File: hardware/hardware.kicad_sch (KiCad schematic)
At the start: 39 parts, among them J1 USB_C_Receptacle_USB2.0, J2 Conn_01x12_Pin, J4 Conn_01x12_Pin, SW1 RST, SW2 BOOT, U1 ESP32-C3-MINI-1, U2 CH217K, U3 AMS1117-3.3, U4 DHT11, U5 BMP280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

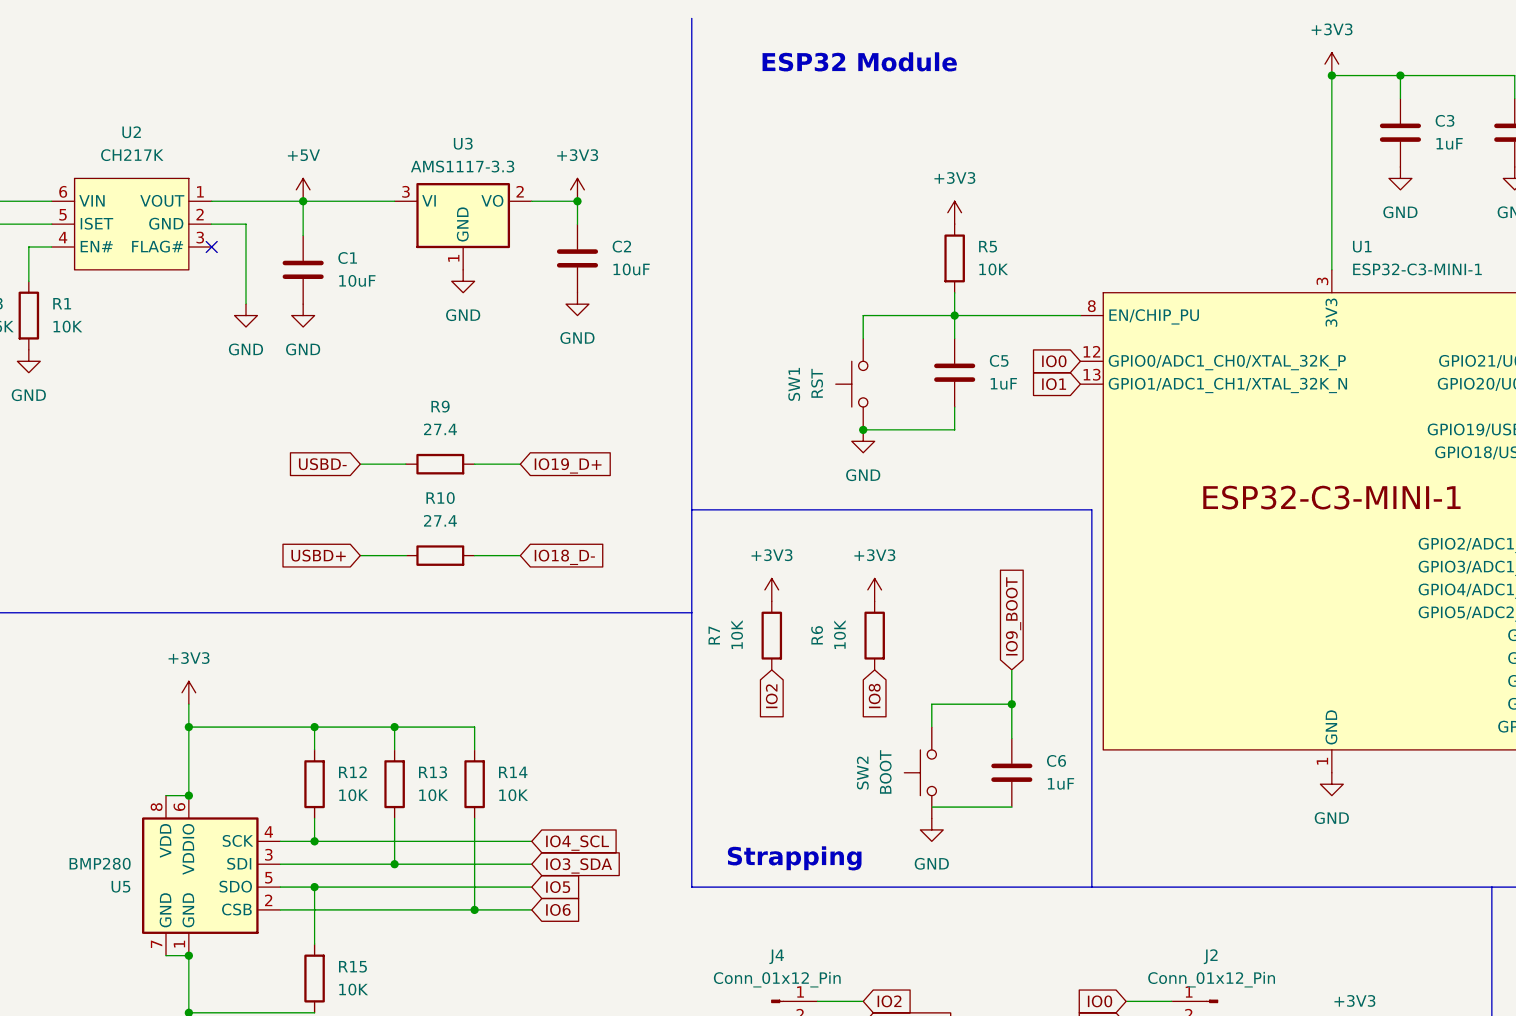
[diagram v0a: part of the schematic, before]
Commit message: Auto routing for PCB by free-routing.
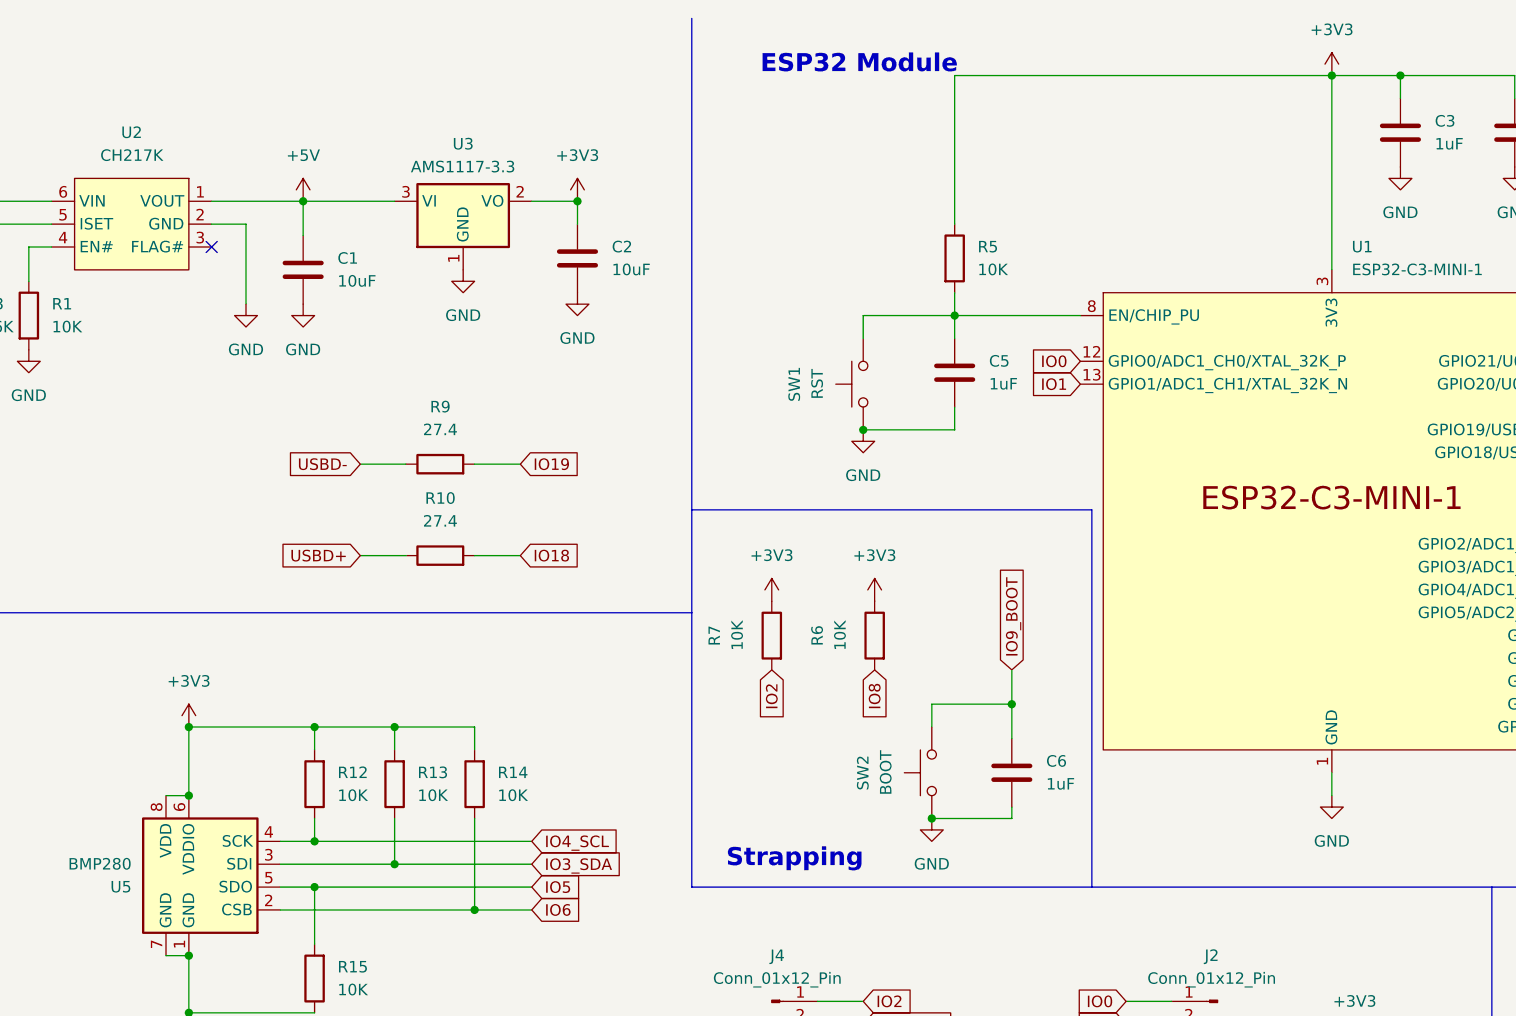
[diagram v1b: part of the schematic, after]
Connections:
- net IO18_D- is gone; now on net IO18: R10.2
- net IO19_D+ is gone; now on net IO19: R9.2
- net GND: now also C6.2

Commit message: Draft version to enable stepper.
And have some changes on KiCad data, may have something wrong. Let's just keep them now.
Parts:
- removed R1: 10K, Resistor_SMD:R_0402_1005Metric, symbol Device:R
- removed R3: 56K, Resistor_SMD:R_0402_1005Metric, symbol Device:R
- removed U2: CH217K, Package_TO_SOT_SMD:SOT-23-6, symbol wch_mcu_peripheral:CH217K
- C1, C2: footprint Capacitor_SMD:C_0402_1005Metric -> Capacitor_SMD:C_0805_2012Metric
- C7: value 0.1uF -> 100nF
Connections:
- net +5V: now also J1.A4 (VBUS), J1.A9 (VBUS), J1.B4 (VBUS), J1.B9 (VBUS)
- no-connect marks 6 -> 5
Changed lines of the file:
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@@
   (no_connect (at 41.91 59.69))
   (no_connect (at 271.78 123.19))
-  (no_connect (at 93.98 36.83))
   (wire (pts (xy 26.67 158.75) (xy 21.59 158.75))
     (stroke (width 0) (type default))
@@
     (stroke (width 0) (type default))
   )
-  (wire (pts (xy 66.04 34.29) (xy 66.04 40.64))
-    (stroke (width 0) (type default))
-  )
   (wire (pts (xy 104.14 31.75) (xy 104.14 35.56))
     (stroke (width 0) (type default))
@@
     (stroke (width 0) (type default))
   )
-  (wire (pts (xy 97.79 34.29) (xy 97.79 43.18))
-    (stroke (width 0) (type default))
-  )
   (wire (pts (xy 226.06 17.78) (xy 238.76 17.78))
     (stroke (width 0) (type default))
@@
     (stroke (width 0) (type default))
   )
-  (wire (pts (xy 93.98 34.29) (xy 97.79 34.29))
-    (stroke (width 0) (type default))
-  )
   (wire (pts (xy 246.38 59.69) (xy 248.92 59.69))
     (stroke (width 0) (type default))
@@
     (stroke (width 0) (type default))
   )
-  (wire (pts (xy 73.66 36.83) (xy 73.66 40.64))
-    (stroke (width 0) (type default))
-  )
   (wire (pts (xy 101.6 110.49) (xy 123.19 110.49))
     (stroke (width 0) (type default))
@@
     (stroke (width 0) (type default))
   )
-  (wire (pts (xy 76.2 36.83) (xy 73.66 36.83))
-    (stroke (width 0) (type default))
-  )
   (wire (pts (xy 49.53 153.67) (xy 49.53 152.4))
     (stroke (width 0) (type default))
@@
     (stroke (width 0) (type default))
   )
-  (wire (pts (xy 41.91 31.75) (xy 76.2 31.75))
+  (wire (pts (xy 41.91 31.75) (xy 104.14 31.75))
     (stroke (width 0) (type default))
   )
@@
     (stroke (width 0) (type default))
   )
-  (wire (pts (xy 76.2 34.29) (xy 66.04 34.29))
-    (stroke (width 0) (type default))
-  )
   (wire (pts (xy 161.29 125.73) (xy 166.37 125.73))
     (stroke (width 0) (type default))
@@
   )
   (wire (pts (xy 105.41 92.71) (xy 105.41 90.17))
-    (stroke (width 0) (type default))
-  )
-  (wire (pts (xy 93.98 31.75) (xy 104.14 31.75))
     (stroke (width 0) (type default))
   )
@@
       (effects (font (size 1.27 1.27)) (justify left))
     )
-    (property "Footprint" "Capacitor_SMD:C_0402_1005Metric" (at 105.1052 43.18 0)
+    (property "Footprint" "Capacitor_SMD:C_0805_2012Metric" (at 105.1052 43.18 0)
       (effects (font (size 1.27 1.27)) hide)
     )
@@
     )
   )
-  (symbol (lib_id "Device:R") (at 73.66 44.45 0) (unit 1)
-    (in_bom yes) (on_board yes) (dnp no) (fields_autoplaced)
-    (property "Reference" "R1" (at 76.2 43.18 0)
-      (effects (font (size 1.27 1.27)) (justify left))
-    )
-    (property "Value" "10K" (at 76.2 45.72 0)
-      (effects (font (size 1.27 1.27)) (justify left))
-    )
-    (property "Footprint" "Resistor_SMD:R_0402_1005Metric" (at 71.882 44.45 90)
-      (effects (font (size 1.27 1.27)) hide)
-    )
-    (property "Datasheet" "~" (at 73.66 44.45 0)
-      (effects (font (size 1.27 1.27)) hide)
-    )
-    (pin "1")
-    (pin "2")
-    (instances
-      (project "hardware"
-        (path "/d72f8024-ddb5-42d1-8bba-6f155975e95c"
-          (reference "R1") (unit 1)
-        )
-      )
-    )
-  )
   (symbol (lib_id "Device:R") (at 58.42 63.5 0) (unit 1)
     (in_bom yes) (on_board yes) (dnp no) (fields_autoplaced)
@@
     )
   )
-  (symbol (lib_id "power:GND") (at 66.04 48.26 0) (unit 1)
-    (in_bom yes) (on_board yes) (dnp no) (fields_autoplaced)
-    (property "Reference" "#PWR01" (at 66.04 54.61 0)
-      (effects (font (size 1.27 1.27)) hide)
-    )
-    (property "Value" "GND" (at 66.04 53.34 0)
-      (effects (font (size 1.27 1.27)))
-    )
-    (property "Footprint" "" (at 66.04 48.26 0)
-      (effects (font (size 1.27 1.27)) hide)
-    )
-    (property "Datasheet" "" (at 66.04 48.26 0)
-      (effects (font (size 1.27 1.27)) hide)
-    )
-    (pin "1")
-    (instances
-      (project "hardware"
-        (path "/d72f8024-ddb5-42d1-8bba-6f155975e95c"
-          (reference "#PWR01") (unit 1)
-        )
-      )
-    )
-  )
   (symbol (lib_id "Device:R") (at 119.38 60.96 90) (unit 1)
     (in_bom yes) (on_board yes) (dnp no) (fields_autoplaced)
@@
       (effects (font (size 1.27 1.27)) (justify left))
     )
-    (property "Footprint" "Capacitor_SMD:C_0402_1005Metric" (at 135.5852 41.91 0)
+    (property "Footprint" "Capacitor_SMD:C_0805_2012Metric" (at 135.5852 41.91 0)
       (effects (font (size 1.27 1.27)) hide)
     )
@@
         (path "/d72f8024-ddb5-42d1-8bba-6f155975e95c"
           (reference "C6") (unit 1)
-        )
-      )
-    )
-  )
-  (symbol (lib_id "power:GND") (at 73.66 48.26 0) (unit 1)
-    (in_bom yes) (on_board yes) (dnp no) (fields_autoplaced)
-    (property "Reference" "#PWR03" (at 73.66 54.61 0)
-      (effects (font (size 1.27 1.27)) hide)
-    )
-    (property "Value" "GND" (at 73.66 53.34 0)
-      (effects (font (size 1.27 1.27)))
-    )
-    (property "Footprint" "" (at 73.66 48.26 0)
-      (effects (font (size 1.27 1.27)) hide)
-    )
-    (property "Datasheet" "" (at 73.66 48.26 0)
-      (effects (font (size 1.27 1.27)) hide)
-    )
-    (pin "1")
-    (instances
-      (project "hardware"
-        (path "/d72f8024-ddb5-42d1-8bba-6f155975e95c"
-          (reference "#PWR03") (unit 1)
         )
       )
@@
       (effects (font (size 1.27 1.27)) (justify left))
     )
-    (property "Value" "0.1uF" (at 62.23 166.37 0)
+    (property "Value" "100nF" (at 62.23 166.37 0)
       (effects (font (size 1.27 1.27)) (justify left))
     )
@@
     )
   )
-  (symbol (lib_id "power:GND") (at 97.79 43.18 0) (unit 1)
-    (in_bom yes) (on_board yes) (dnp no) (fields_autoplaced)
-    (property "Reference" "#PWR05" (at 97.79 49.53 0)
-      (effects (font (size 1.27 1.27)) hide)
-    )
-    (property "Value" "GND" (at 97.79 48.26 0)
-      (effects (font (size 1.27 1.27)))
-    )
-    (property "Footprint" "" (at 97.79 43.18 0)
-      (effects (font (size 1.27 1.27)) hide)
-    )
-    (property "Datasheet" "" (at 97.79 43.18 0)
-      (effects (font (size 1.27 1.27)) hide)
-    )
-    (pin "1")
-    (instances
-      (project "hardware"
-        (path "/d72f8024-ddb5-42d1-8bba-6f155975e95c"
-          (reference "#PWR05") (unit 1)
-        )
-      )
-    )
-  )
   (symbol (lib_id "power:+3V3") (at 264.16 115.57 0) (unit 1)
     (in_bom yes) (on_board yes) (dnp no) (fields_autoplaced)
@@
     )
   )
-  (symbol (lib_id "wch_mcu_peripheral:CH217K") (at 85.09 34.29 0) (mirror y) (unit 1)
-    (in_bom yes) (on_board yes) (dnp no)
-    (property "Reference" "U2" (at 85.09 24.13 0)
-      (effects (font (size 1.27 1.27)))
-    )
-    (property "Value" "CH217K" (at 85.09 26.67 0)
-      (effects (font (size 1.27 1.27)))
-    )
-    (property "Footprint" "Package_TO_SOT_SMD:SOT-23-6" (at 87.63 44.45 0)
-      (effects (font (size 1.27 1.27)) hide)
-    )
-    (property "Datasheet" "" (at 91.44 39.37 0)
-      (effects (font (size 1.27 1.27)) hide)
-    )
-    (pin "3")
-    (pin "1")
-    (pin "5")
-    (pin "6")
-    (pin "4")
-    (pin "2")
-    (instances
-      (project "hardware"
-        (path "/d72f8024-ddb5-42d1-8bba-6f155975e95c"
-          (reference "U2") (unit 1)
-        )
-      )
-    )
-  )
   (symbol (lib_id "Sensor:DHT11") (at 30.48 102.87 0) (unit 1)
     (in_bom yes) (on_board yes) (dnp no) (fields_autoplaced)
@@
         )
       )
-    )
-  )
-  (symbol (lib_id "Device:R") (at 66.04 44.45 0) (unit 1)
-    (in_bom yes) (on_board yes) (dnp no) (fields_autoplaced)
-    (property "Reference" "R3" (at 68.58 43.18 0)
-      (effects (font (size 1.27 1.27)) (justify left))
-    )
-    (property "Value" "56K" (at 68.58 45.72 0)
-      (effects (font (size 1.27 1.27)) (justify left))
-    )
-    (property "Footprint" "Resistor_SMD:R_0402_1005Metric" (at 64.262 44.45 90)
-      (effects (font (size 1.27 1.27)) hide)
-    )
-    (property "Datasheet" "~" (at 66.04 44.45 0)
-      (effects (font (size 1.27 1.27)) hide)
-    )
-    (pin "1")
-    (pin "2")
-    (instances
-      (project "hardware"
-        (path "/d72f8024-ddb5-42d1-8bba-6f155975e95c"
-          (reference "R3") (unit 1)
-        )
-      )
